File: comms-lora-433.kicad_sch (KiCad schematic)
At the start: 11 parts, among them J4 Conn_Coaxial_Small, U9 RFM96W-433S2

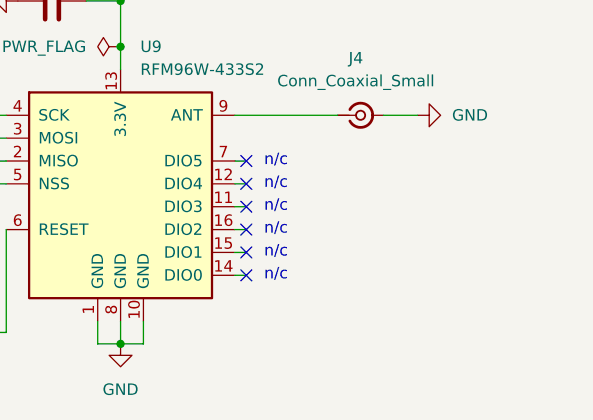
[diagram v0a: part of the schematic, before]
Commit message: Added mounting holes
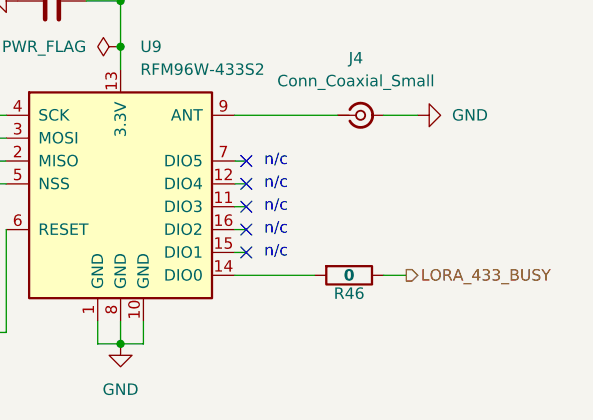
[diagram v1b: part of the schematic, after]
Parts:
- added R46: 0, Resistor_SMD:R_0603_1608Metric, symbol Device:R
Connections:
- net at U9.14 (DIO0): now also R46.2
- new net LORA_433_BUSY: R46.1
- no-connect marks 6 -> 5
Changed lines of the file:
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@@
-	)
-	(no_connect
-		(at 170.18 110.49)
 	)
 	(no_connect
@@
 	(wire
 		(pts
+			(xy 185.42 110.49) (xy 187.96 110.49)
+		)
+		(stroke
+			(width 0)
+			(type default)
+		)
+	)
+	(wire
+		(pts
 			(xy 185.42 92.71) (xy 189.23 92.71)
 		)
@@
 	(wire
 		(pts
+			(xy 168.91 110.49) (xy 177.8 110.49)
+		)
+		(stroke
+			(width 0)
+			(type default)
+		)
+	)
+	(wire
+		(pts
 			(xy 139.7 97.79) (xy 143.51 97.79)
 		)
@@
 		(pts
 			(xy 152.4 80.01) (xy 156.21 80.01)
-		)
-		(stroke
-			(width 0)
-			(type default)
-		)
-	)
-	(wire
-		(pts
-			(xy 168.91 110.49) (xy 170.18 110.49)
 		)
 		(stroke
@@
 	(text "n/c"
 		(exclude_from_sim no)
-		(at 173.482 110.49 0)
-		(effects
-			(font
-				(size 1.27 1.27)
-			)
-		)
-	)
-	(text "n/c"
-		(exclude_from_sim no)
 		(at 173.482 107.95 0)
 		(effects
@@
 			)
 			(justify right bottom)
+		)
+	)
+	(hierarchical_label "LORA_433_BUSY"
+		(shape output)
+		(at 187.96 110.49 0)
+		(fields_autoplaced yes)
+		(effects
+			(font
+				(size 1.27 1.27)
+			)
+			(justify left)
 		)
 	)
@@
 					(unit 1)
 				)
+			)
+		)
+	)
+	(symbol
+		(lib_id "Device:R")
+		(at 181.61 110.49 270)
+		(unit 1)
+		(exclude_from_sim no)
+		(in_bom yes)
+		(on_board yes)
+		(dnp no)
+		(property "Reference" "R46"
+			(at 181.61 112.522 90)
+			(effects
+				(font
+					(size 1.27 1.27)
+				)
+			)
+		)
+		(property "Value" "0"
+			(at 181.61 110.49 90)
+			(effects
+				(font
+					(size 1.27 1.27)
+					(thickness 0.254)
+					(bold yes)
+				)
+			)
+		)
+		(property "Footprint" "Resistor_SMD:R_0603_1608Metric"
+			(at 181.61 108.712 90)
+			(effects
+				(font
+					(size 1.27 1.27)
+				)
+				(hide yes)
+			)
+		)
+		(property "Datasheet" "Datasheet"
+			(at 181.61 110.49 0)
+			(effects
+				(font
+					(size 1.27 1.27)
+				)
+				(hide yes)
+			)
+		)
+		(property "Description" "Resistor"
+			(at 181.61 110.49 0)
+			(effects
+				(font
+					(size 1.27 1.27)
+				)
+				(hide yes)
+			)
+		)
+		(property "Mfr" "YAGEO"
+			(at 181.61 110.49 0)
+			(effects
+				(font
+					(size 1.27 1.27)
+				)
+				(hide yes)
+			)
+		)
+		(property "Mfr P/N" "RC0603JR-070RL"
+			(at 181.61 110.49 0)
+			(effects
+				(font
+					(size 1.27 1.27)
+				)
+				(hide yes)
+			)
+		)
+		(property "Supplier_1" "Digikey"
+			(at 181.61 110.49 0)
+			(effects
+				(font
+					(size 1.27 1.27)
+				)
+				(hide yes)
+			)
+		)
+		(property "Supplier_1 P/N" "311-0.0GRCT-ND"
+			(at 181.61 110.49 0)
+			(effects
+				(font
+					(size 1.27 1.27)
+				)
+				(hide yes)
+			)
+		)
+		(property "Supplier_1 Unit Price" "$0.10000 "
+			(at 181.61 110.49 0)
+			(effects
+				(font
+					(size 1.27 1.27)
+				)
+				(hide yes)
+			)
+		)
+		(property "Supplier_1 Price @ Qty" "$0.00304 "
+			(at 181.61 110.49 0)
+			(effects
+				(font
+					(size 1.27 1.27)
+				)
+				(hide yes)
+			)
+		)
+		(property "Supplier_2" ""
+			(at 181.61 110.49 0)
+			(effects
+				(font
+					(size 1.27 1.27)
+				)
+				(hide yes)
+			)
+		)
+		(property "Supplier_2 P/N" ""
+			(at 181.61 110.49 0)
+			(effects
+				(font
+					(size 1.27 1.27)
+				)
+				(hide yes)
+			)
+		)
+		(property "Supplier_2 Unit Price" ""
+			(at 181.61 110.49 0)
+			(effects
+				(font
+					(size 1.27 1.27)
+				)
+				(hide yes)
+			)
+		)
+		(property "Supplier_2 Price @ Qty" ""
+			(at 181.61 110.49 0)
+			(effects
+				(font
+					(size 1.27 1.27)
+				)
+				(hide yes)
+			)
+		)
+		(pin "1"
+		)
+		(pin "2"
+		)
+		(instances
+			(project "roamer"
+				(path "/1c59de6a-87fe-4223-8898-4b0383164a31/27e0c772-2e0b-4398-8c51-a65e2e356334"
+					(reference "R46")
+					(unit 1)
+				)

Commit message: Creating fab package
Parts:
- J4: Supplier_1 Price @ Qty $0.38945 -> 0.38945; Supplier_1 Unit Price $0.94000 -> 0.94000
- R12, R13, R14, R15, R39, R45, R46: Supplier_1 Price @ Qty $0.00304 -> 0.00304; Supplier_1 Unit Price $0.10000 -> 0.10000
- U9: Mfr (none) -> Adafruit Industries LLC; Mfr P/N (none) -> 3073; Supplier_1 (none) -> Digikey; Supplier_1 P/N (none) -> 1528-1668-ND; Supplier_1 Price @ Qty (none) -> 19.95000; Supplier_1 Unit Price (none) -> 19.95000
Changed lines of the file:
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@@
 			)
 		)
-		(property "Supplier_1 Unit Price" "$0.94000 "
+		(property "Supplier_1 Unit Price" "0.94000 "
 			(at 182.88 92.71 0)
 			(effects
@@
 			)
 		)
-		(property "Supplier_1 Price @ Qty" "$0.38945 "
+		(property "Supplier_1 Price @ Qty" "0.38945 "
 			(at 182.88 92.71 0)
 			(effects
@@
 			)
 		)
-		(property "Supplier_1 Unit Price" "$0.10000 "
+		(property "Supplier_1 Unit Price" "0.10000 "
 			(at 135.89 92.71 0)
 			(effects
@@
 			)
 		)
-		(property "Supplier_1 Price @ Qty" "$0.00304 "
+		(property "Supplier_1 Price @ Qty" "0.00304 "
 			(at 135.89 92.71 0)
 			(effects
@@
 	(symbol
 		(lib_id "Device:R")
+		(at 135.89 97.79 270)
+		(unit 1)
+		(exclude_from_sim no)
+		(in_bom yes)
+		(on_board yes)
+		(dnp no)
+		(property "Reference" "R14"
+			(at 132.08 96.266 90)
+			(effects
+				(font
+					(size 1.27 1.27)
+				)
+			)
+		)
+		(property "Value" "0"
+			(at 135.89 97.79 90)
+			(effects
+				(font
+					(size 1.27 1.27)
+					(thickness 0.254)
+					(bold yes)
+				)
+			)
+		)
+		(property "Footprint" "Resistor_SMD:R_0603_1608Metric"
+			(at 135.89 96.012 90)
+			(effects
+				(font
+					(size 1.27 1.27)
+				)
+				(hide yes)
+			)
+		)
+		(property "Datasheet" "Datasheet"
+			(at 135.89 97.79 0)
+			(effects
+				(font
+					(size 1.27 1.27)
+				)
+				(hide yes)
+			)
+		)
+		(property "Description" "Resistor"
+			(at 135.89 97.79 0)
+			(effects
+				(font
+					(size 1.27 1.27)
+				)
+				(hide yes)
+			)
+		)
+		(property "Mfr" "YAGEO"
+			(at 135.89 97.79 0)
+			(effects
+				(font
+					(size 1.27 1.27)
+				)
+				(hide yes)
+			)
+		)
+		(property "Mfr P/N" "RC0603JR-070RL"
+			(at 135.89 97.79 0)
+			(effects
+				(font
+					(size 1.27 1.27)
+				)
+				(hide yes)
+			)
+		)
+		(property "Supplier_1" "Digikey"
+			(at 135.89 97.79 0)
+			(effects
+				(font
+					(size 1.27 1.27)
+				)
+				(hide yes)
+			)
+		)
+		(property "Supplier_1 P/N" "311-0.0GRCT-ND"
+			(at 135.89 97.79 0)
+			(effects
+				(font
+					(size 1.27 1.27)
+				)
+				(hide yes)
+			)
+		)
+		(property "Supplier_1 Unit Price" "0.10000 "
+			(at 135.89 97.79 0)
+			(effects
+				(font
+					(size 1.27 1.27)
+				)
+				(hide yes)
+			)
+		)
+		(property "Supplier_1 Price @ Qty" "0.00304 "
+			(at 135.89 97.79 0)
+			(effects
+				(font
+					(size 1.27 1.27)
+				)
+				(hide yes)
+			)
+		)
+		(property "Supplier_2" ""
+			(at 135.89 97.79 0)
+			(effects
+				(font
+					(size 1.27 1.27)
+				)
+				(hide yes)
+			)
+		)
+		(property "Supplier_2 P/N" ""
+			(at 135.89 97.79 0)
+			(effects
+				(font
+					(size 1.27 1.27)
+				)
+				(hide yes)
+			)
+		)
+		(property "Supplier_2 Unit Price" ""
+			(at 135.89 97.79 0)
+			(effects
+				(font
+					(size 1.27 1.27)
+				)
+				(hide yes)
+			)
+		)
+		(property "Supplier_2 Price @ Qty" ""
+			(at 135.89 97.79 0)
+			(effects
+				(font
+					(size 1.27 1.27)
+				)
+				(hide yes)
+			)
+		)
+		(pin "1"
+		)
+		(pin "2"
+		)
+		(instances
+			(project "roamer"
+				(path "/1c59de6a-87fe-4223-8898-4b0383164a31/27e0c772-2e0b-4398-8c51-a65e2e356334"
+					(reference "R14")
+					(unit 1)
+				)
+			)
+		)
+	)
+	(symbol
+		(lib_id "Device:R")
 		(at 135.89 101.6 270)
 		(unit 1)
@@
 			)
 		)
-		(property "Supplier_1 Unit Price" "$0.10000 "
+		(property "Supplier_1 Unit Price" "0.10000 "
 			(at 135.89 101.6 0)
 			(effects
@@
 			)
 		)
-		(property "Supplier_1 Price @ Qty" "$0.00304 "
+		(property "Supplier_1 Price @ Qty" "0.00304 "
 			(at 135.89 101.6 0)
 			(effects
@@
 			)
 		)
-		(property "Mfr" ""
+		(property "Mfr" "Adafruit Industries LLC"
 			(at 156.21 100.33 0)
 			(effects
@@
 			)
 		)
-		(property "Mfr P/N" ""
+		(property "Mfr P/N" "3073"
 			(at 156.21 100.33 0)
 			(effects
@@
 			)
 		)
-		(property "Supplier_1" ""
+		(property "Supplier_1" "Digikey"
 			(at 156.21 100.33 0)
 			(effects
@@
 			)
 		)
-		(property "Supplier_1 P/N" ""
+		(property "Supplier_1 P/N" "1528-1668-ND"
 			(at 156.21 100.33 0)
 			(effects
@@
 			)
 		)
-		(property "Supplier_1 Unit Price" ""
+		(property "Supplier_1 Unit Price" "19.95000"
 			(at 156.21 100.33 0)
 			(effects
@@
 			)
 		)
-		(property "Supplier_1 Price @ Qty" ""
+		(property "Supplier_1 Price @ Qty" "19.95000"
 			(at 156.21 100.33 0)
 			(effects
@@
 				(path "/1c59de6a-87fe-4223-8898-4b0383164a31/27e0c772-2e0b-4398-8c51-a65e2e356334"
 					(reference "U9")
-					(unit 1)
-				)
-			)
-		)
-	)
-	(symbol
-		(lib_id "Device:R")
-		(at 135.89 97.79 270)
-		(unit 1)
-		(exclude_from_sim no)
-		(in_bom yes)
-		(on_board yes)
-		(dnp no)
-		(property "Reference" "R14"
-			(at 132.08 96.266 90)
-			(effects
-				(font
-					(size 1.27 1.27)
-				)
-			)
-		)
-		(property "Value" "0"
-			(at 135.89 97.79 90)
-			(effects
-				(font
-					(size 1.27 1.27)
-					(thickness 0.254)
-					(bold yes)
-				)
-			)
-		)
-		(property "Footprint" "Resistor_SMD:R_0603_1608Metric"
-			(at 135.89 96.012 90)
-			(effects
-				(font
-					(size 1.27 1.27)
-				)
-				(hide yes)
-			)
-		)
-		(property "Datasheet" "Datasheet"
-			(at 135.89 97.79 0)
-			(effects
-				(font
-					(size 1.27 1.27)
-				)
-				(hide yes)
-			)
-		)
-		(property "Description" "Resistor"
-			(at 135.89 97.79 0)
-			(effects
-				(font
-					(size 1.27 1.27)
-				)
-				(hide yes)
-			)
-		)
-		(property "Mfr" "YAGEO"
-			(at 135.89 97.79 0)
-			(effects
-				(font
-					(size 1.27 1.27)
-				)
-				(hide yes)
-			)
-		)
-		(property "Mfr P/N" "RC0603JR-070RL"
-			(at 135.89 97.79 0)
-			(effects
-				(font
-					(size 1.27 1.27)
-				)
-				(hide yes)
-			)
-		)
-		(property "Supplier_1" "Digikey"
-			(at 135.89 97.79 0)
-			(effects
-				(font
-					(size 1.27 1.27)
-				)
-				(hide yes)
-			)
-		)
-		(property "Supplier_1 P/N" "311-0.0GRCT-ND"
-			(at 135.89 97.79 0)
-			(effects
-				(font
-					(size 1.27 1.27)
-				)
-				(hide yes)
-			)
-		)
-		(property "Supplier_1 Unit Price" "$0.10000 "
-			(at 135.89 97.79 0)
-			(effects
-				(font
-					(size 1.27 1.27)
-				)
-				(hide yes)
-			)
-		)
-		(property "Supplier_1 Price @ Qty" "$0.00304 "
-			(at 135.89 97.79 0)
-			(effects
-				(font
-					(size 1.27 1.27)
-				)
-				(hide yes)
-			)
-		)
-		(property "Supplier_2" ""
-			(at 135.89 97.79 0)
-			(effects
-				(font
-					(size 1.27 1.27)
-				)
-				(hide yes)
-			)
-		)
-		(property "Supplier_2 P/N" ""
-			(at 135.89 97.79 0)
-			(effects
-				(font
-					(size 1.27 1.27)
-				)
-				(hide yes)
-			)
-		)
-		(property "Supplier_2 Unit Price" ""
-			(at 135.89 97.79 0)
-			(effects
-				(font
-					(size 1.27 1.27)
-				)
-				(hide yes)
-			)
-		)
-		(property "Supplier_2 Price @ Qty" ""
-			(at 135.89 97.79 0)
-			(effects
-				(font
-					(size 1.27 1.27)
-				)
-				(hide yes)
-			)
-		)
-		(pin "1"
-		)
-		(pin "2"
-		)
-		(instances
-			(project "roamer"
-				(path "/1c59de6a-87fe-4223-8898-4b0383164a31/27e0c772-2e0b-4398-8c51-a65e2e356334"
-					(reference "R14")
 					(unit 1)
 				)
@@
 			)
 		)
-		(property "Supplier_1 Unit Price" "$0.10000 "
+		(property "Supplier_1 Unit Price" "0.10000 "
 			(at 135.89 95.25 0)
 			(effects
@@
 			)
 		)
-		(property "Supplier_1 Price @ Qty" "$0.00304 "
+		(property "Supplier_1 Price @ Qty" "0.00304 "
 			(at 135.89 95.25 0)
 			(effects
@@
 			)
 		)
-		(property "Supplier_1 Unit Price" "$0.10000 "
+		(property "Supplier_1 Unit Price" "0.10000 "
 			(at 156.21 71.12 0)
 			(effects
@@
 			)
 		)
-		(property "Supplier_1 Price @ Qty" "$0.00304 "
+		(property "Supplier_1 Price @ Qty" "0.00304 "
 			(at 156.21 71.12 0)
 			(effects
@@
 			)
 		)
-		(property "Supplier_1 Unit Price" "$0.10000 "
+		(property "Supplier_1 Unit Price" "0.10000 "
 			(at 181.61 110.49 0)
 			(effects
@@
 			)
 		)
-		(property "Supplier_1 Price @ Qty" "$0.00304 "
+		(property "Supplier_1 Price @ Qty" "0.00304 "
 			(at 181.61 110.49 0)
 			(effects
@@
 			)
 		)
-		(property "Supplier_1 Unit Price" "$0.10000 "
+		(property "Supplier_1 Unit Price" "0.10000 "
 			(at 135.89 116.84 0)
 			(effects
@@
 			)
 		)
-		(property "Supplier_1 Price @ Qty" "$0.00304 "
+		(property "Supplier_1 Price @ Qty" "0.00304 "
 			(at 135.89 116.84 0)
 			(effects

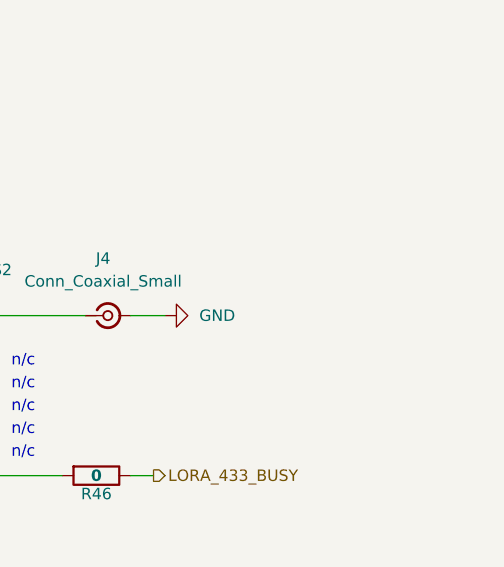
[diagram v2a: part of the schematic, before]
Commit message: Updating silkscreen comments
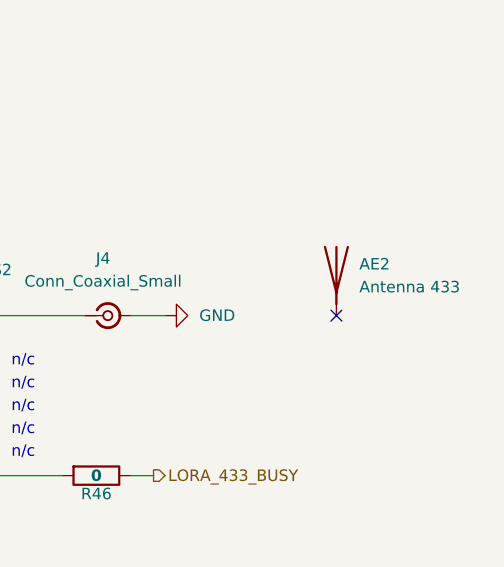
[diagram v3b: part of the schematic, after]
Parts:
- added AE2: Antenna 433, symbol Device:Antenna
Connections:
- no-connect marks 5 -> 6
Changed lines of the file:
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@@
+	)
+	(no_connect
+		(at 208.28 92.71)
 	)
 	(no_connect
@@
 					(unit 1)
 				)
+			)
+		)
+	)
+	(symbol
+		(lib_id "Device:Antenna")
+		(at 208.28 87.63 0)
+		(unit 1)
+		(exclude_from_sim no)
+		(in_bom yes)
+		(on_board yes)
+		(dnp no)
+		(fields_autoplaced yes)
+		(property "Reference" "AE2"
+			(at 210.82 86.9949 0)
+			(effects
+				(font
+					(size 1.27 1.27)
+				)
+				(justify left)
+			)
+		)
+		(property "Value" "Antenna 433"
+			(at 210.82 89.5349 0)
+			(effects
+				(font
+					(size 1.27 1.27)
+				)
+				(justify left)
+			)
+		)
+		(property "Footprint" ""
+			(at 208.28 87.63 0)
+			(effects
+				(font
+					(size 1.27 1.27)
+				)
+				(hide yes)
+			)
+		)
+		(property "Datasheet" "Datasheet"
+			(at 208.28 87.63 0)
+			(effects
+				(font
+					(size 1.27 1.27)
+				)
+				(hide yes)
+			)
+		)
+		(property "Description" "RF ANT 433MHZ WHIP STR CAB PAN"
+			(at 208.28 87.63 0)
+			(effects
+				(font
+					(size 1.27 1.27)
+				)
+				(hide yes)
+			)
+		)
+		(property "Mfr" "TE Connectivity Linx"
+			(at 208.28 87.63 0)
+			(effects
+				(font
+					(size 1.27 1.27)
+				)
+				(hide yes)
+			)
+		)
+		(property "Mfr P/N" "ANT-433-PW-QW-UFL"
+			(at 208.28 87.63 0)
+			(effects
+				(font
+					(size 1.27 1.27)
+				)
+				(hide yes)
+			)
+		)
+		(property "Supplier_1" "DigiKey"
+			(at 208.28 87.63 0)
+			(effects
+				(font
+					(size 1.27 1.27)
+				)
+				(hide yes)
+			)
+		)
+		(property "Supplier_1 P/N" "ANT-433-PW-QW-UFL-ND"
+			(at 208.28 87.63 0)
+			(effects
+				(font
+					(size 1.27 1.27)
+				)
+				(hide yes)
+			)
+		)
+		(property "Supplier_1 Unit Price" "11.79000"
+			(at 208.28 87.63 0)
+			(effects
+				(font
+					(size 1.27 1.27)
+				)
+				(hide yes)
+			)
+		)
+		(property "Supplier_1 Price @ Qty" "10.94008"
+			(at 208.28 87.63 0)
+			(effects
+				(font
+					(size 1.27 1.27)
+				)
+				(hide yes)
+			)
+		)
+		(property "Supplier_2" ""
+			(at 208.28 87.63 0)
+			(effects
+				(font
+					(size 1.27 1.27)
+				)
+				(hide yes)
+			)
+		)
+		(property "Supplier_2 P/N" ""
+			(at 208.28 87.63 0)
+			(effects
+				(font
+					(size 1.27 1.27)
+				)
+				(hide yes)
+			)
+		)
+		(property "Supplier_2 Unit Price" ""
+			(at 208.28 87.63 0)
+			(effects
+				(font
+					(size 1.27 1.27)
+				)
+				(hide yes)
+			)
+		)
+		(property "Supplier_2 Price @ Qty" ""
+			(at 208.28 87.63 0)
+			(effects
+				(font
+					(size 1.27 1.27)
+				)
+				(hide yes)
+			)
+		)
+		(pin "1"
+		)
+		(instances
+			(project "roamer"
+				(path "/1c59de6a-87fe-4223-8898-4b0383164a31/27e0c772-2e0b-4398-8c51-a65e2e356334"
+					(reference "AE2")
+					(unit 1)
+				)
